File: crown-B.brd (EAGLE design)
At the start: 302 x 51.5 mm, 15 parts

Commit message: Made B board, looks a bit funky on the routing.
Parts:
- moved PTH2 7.62 mm to (43.9, 58.4)
- moved SKIP-PTH2 7.62 mm to (48.5, 47.5)
- moved C3 7.62 mm to (45.5, 39.6)
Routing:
- net VLIVE: track 179.6 -> 172.0 mm
- net PTH-DO: track 48.9 -> 41.3 mm
- net GND: track 172.9 -> 165.3 mm
- net N$5: track 67.8 -> 65.1 mm
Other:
- outline, holes or cut-outs redrawn

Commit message: Added B plate, which holds battery (best for lipo)
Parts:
- added CN2: (no value), adafruit:JST-PH-2-SMT-RA
- added U$1, U$3, U$4, U$5, U$6, U$7: SMD_BREADBOARD, pcb_crown:SMD_BREADBOARD_4X
- added U$10, U$11, U$12, U$13, U$14, U$15, U$16, U$17, U$22, U$23, U$24, U$25, U$26, U$27, U$28, U$29, U$34, U$35, U$36, U$37, U$38, U$39, U$40, U$41, U$42, U$43, U$44, U$45, U$46, U$47, U$48, U$49, U$50, U$51, U$52, U$53, U$54, U$55, U$56, U$57, U$58, U$59, U$62, U$63, U$64, U$65, U$68, U$69, U$70, U$71: SMD_PAD, pcb_crown:SMD_BREADBOARD_PAD
- moved C3 11.8 mm to (38.7, 49.3), turned to 270 degrees
- moved SKIP-PTH1 10.0 mm to (19.6, 51.6), turned to 90 degrees
- moved C4 9.24 mm to (19.8, 47.5), turned to 90 degrees
- moved SKIP-PTH2 4.61 mm to (49.1, 52.1)
- moved PTH2 0.15 mm to (43.8, 58.4)
- moved PTH1 0.13 mm to (14.5, 58.4)
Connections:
- net PTH-DI renamed PB1
- net SMD-DI renamed PB0
- new net A0: U$2.P$13, U$2.P$32, U$44.P$1, U$55.P$1
- new net A1: U$2.P$14, U$2.P$33, U$43.P$1, U$56.P$1
- new net A2: U$2.P$15, U$2.P$34, U$42.P$1, U$58.P$1
- new net N$11: U$14.P$1, U$15.P$1, U$5.P$3, U$57.P$1
- new net N$12: U$12.P$1, U$13.P$1, U$50.P$1, U$6.P$3
- new net N$13: U$10.P$1, U$11.P$1, U$49.P$1, U$7.P$3
- new net N$14: U$40.P$1, U$41.P$1, U$7.P$7, U$71.P$1
- new net N$15: U$38.P$1, U$39.P$1, U$6.P$7, U$70.P$1
- new net N$16: U$36.P$1, U$37.P$1, U$5.P$7, U$69.P$1
- new net N$17: U$34.P$1, U$35.P$1, U$4.P$7, U$68.P$1
- new net N$2: U$1.P$3, U$24.P$1, U$25.P$1, U$63.P$1
- new net N$20: U$28.P$1, U$29.P$1, U$3.P$7, U$65.P$1
- new net N$21: U$1.P$7, U$26.P$1, U$27.P$1, U$64.P$1
- new net N$22: U$2.P$35
- new net N$6: U$22.P$1, U$23.P$1, U$3.P$3, U$62.P$1
- new net N$9: U$16.P$1, U$17.P$1, U$4.P$3, U$59.P$1
- new net PB2: U$2.P$28, U$2.P$9, U$48.P$1, U$51.P$1
- new net PB3: U$2.P$10, U$2.P$29, U$47.P$1, U$52.P$1
- new net PB4: U$2.P$11, U$2.P$30, U$46.P$1, U$53.P$1
- new net PB5: U$2.P$12, U$2.P$31, U$45.P$1, U$54.P$1
- net GND: now also CN2.2, U$1.P$2, U$2.P$18, U$2.P$37, U$3.P$2, U$4.P$2, U$5.P$2, U$6.P$2, U$7.P$2
- net N$4: now also U$2.P$19
- net PTH-DO: now also U$2.P$38
- net VBAT: now also CN2.1, U$2.P$16
- net VLIVE: now also U$1.P$1, U$2.P$17, U$2.P$36, U$3.P$1, U$4.P$1, U$5.P$1, U$6.P$1, U$7.P$1
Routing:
- net VBAT: track 109.0 -> 295.6 mm, vias 1 -> 3
- net VLIVE: track 172.0 -> 289.4 mm, vias 7 -> 6
- net A2: track 0.00 -> 114.6 mm
- net A1: track 0.00 -> 110.7 mm
- net A0: track 0.00 -> 105.5 mm
- net PB5: track 0.00 -> 103.9 mm
- net PB4: track 0.00 -> 100.6 mm
- net PB3: track 0.00 -> 97.3 mm
- net PB2: track 0.00 -> 93.7 mm
- net GND: track 165.3 -> 213.9 mm, vias 7 -> 5
- net N$4: track 44.6 -> 66.6 mm
- net N$5: track 65.1 -> 44.1 mm
- net PTH-DO: track 41.3 -> 54.7 mm
- net N$9: track 0.00 -> 7.62 mm
- net N$6: track 0.00 -> 7.62 mm
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- added copper zone on layer 1, net GND
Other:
- board size 302 x 51.5 mm -> 57.8 x 50.8 mm
- board text added: "3x Alkaline"
- board text added: "4xNiCAD"
- board text added: "4xNimH"
- board text added: "A4"
- board text added: "A5"
- board text added: "D3"
- board text added: "D4"
- board text added: "D5"
- board text added: "I2C"
- board text added: "LiPo"
- board text added: "RXI"
- board text added: "TXO"

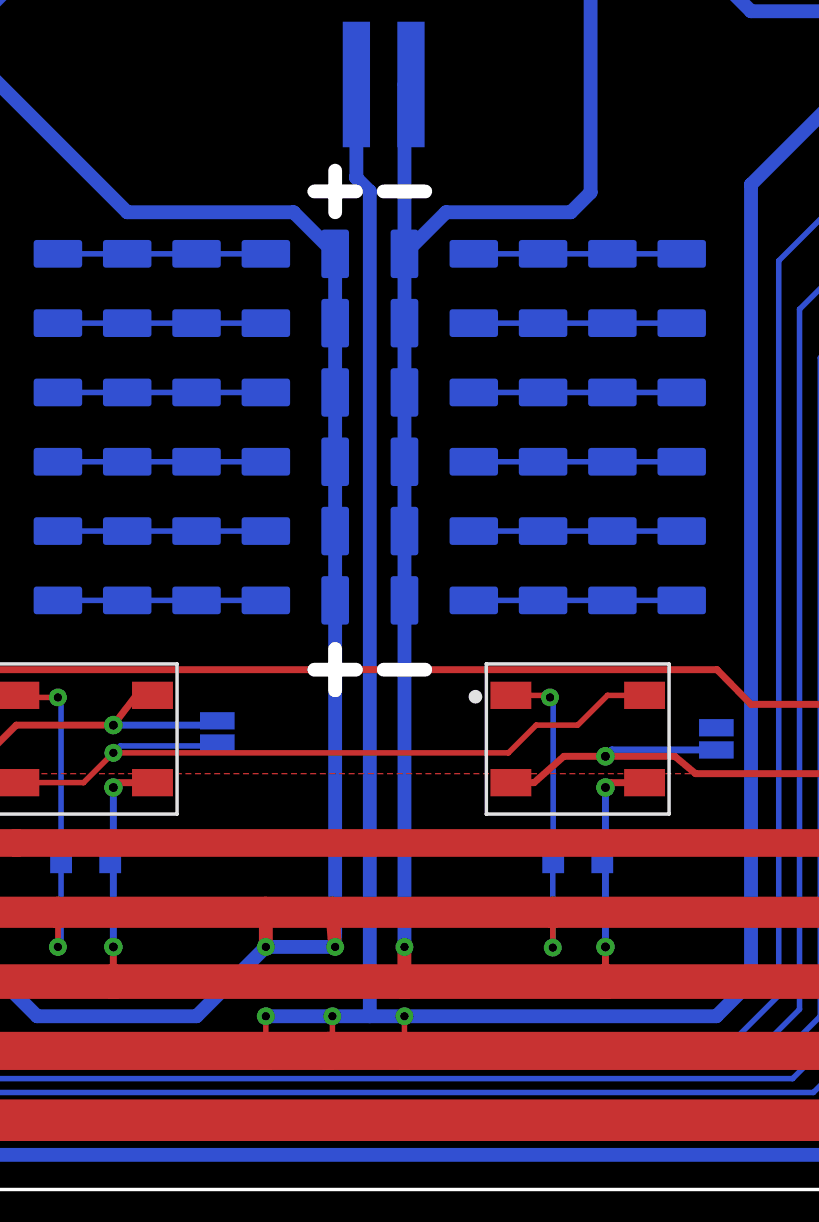
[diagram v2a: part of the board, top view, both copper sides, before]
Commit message: fixed dimension issue
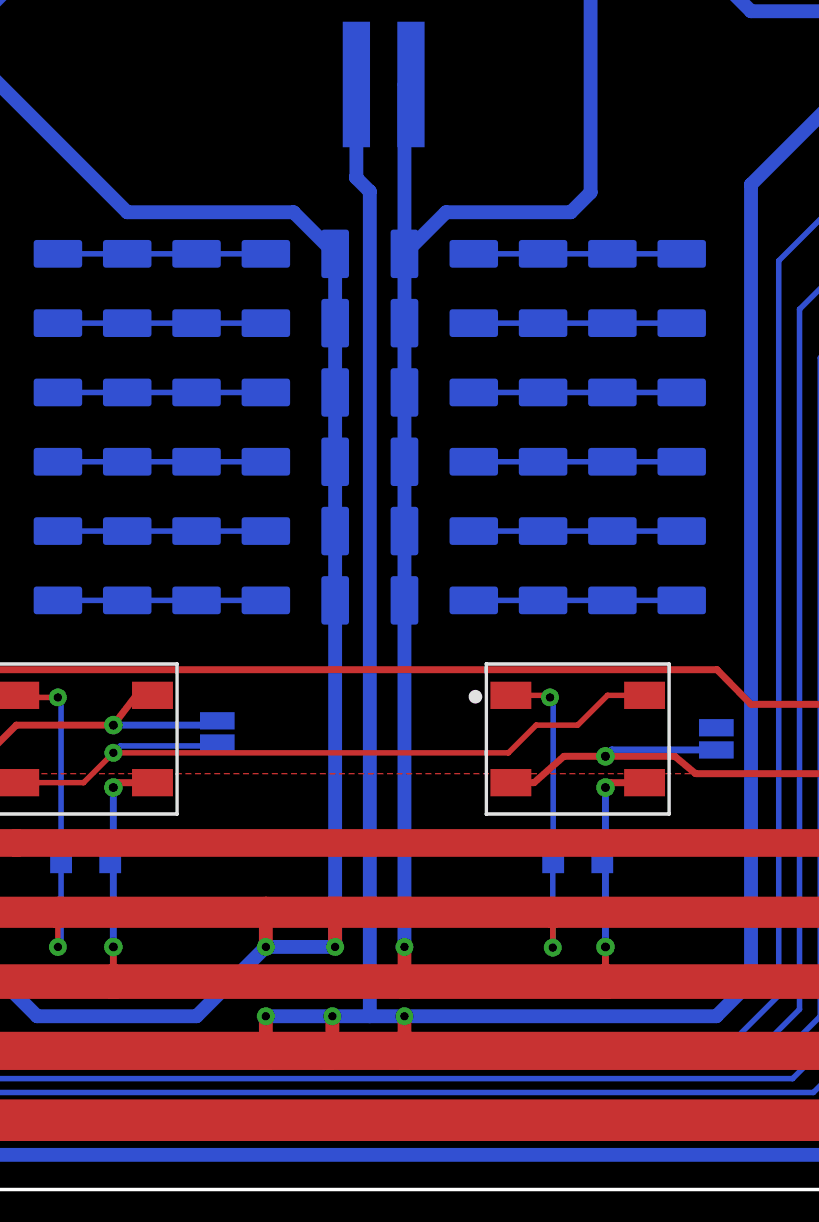
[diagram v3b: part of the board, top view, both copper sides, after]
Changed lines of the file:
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@@
 <grid distance="10" unitdist="mil" unit="mil" style="lines" multiple="5" display="yes" altdistance="1" altunitdist="mil" altunit="mil"/>
 <layers>
-<layer number="1" name="Top" color="4" fill="1" visible="no" active="yes"/>
+<layer number="1" name="Top" color="4" fill="1" visible="yes" active="yes"/>
 <layer number="16" name="Bottom" color="1" fill="1" visible="yes" active="yes"/>
 <layer number="17" name="Pads" color="2" fill="1" visible="yes" active="yes"/>
@@
 <layer number="19" name="Unrouted" color="6" fill="1" visible="yes" active="yes"/>
 <layer number="20" name="Dimension" color="15" fill="1" visible="yes" active="yes"/>
-<layer number="21" name="tPlace" color="16" fill="1" visible="no" active="yes"/>
+<layer number="21" name="tPlace" color="16" fill="1" visible="yes" active="yes"/>
 <layer number="22" name="bPlace" color="14" fill="1" visible="yes" active="yes"/>
 <layer number="23" name="tOrigins" color="15" fill="1" visible="yes" active="yes"/>
 <layer number="24" name="bOrigins" color="15" fill="1" visible="yes" active="yes"/>
 <layer number="25" name="tNames" color="7" fill="1" visible="no" active="yes"/>
-<layer number="26" name="bNames" color="7" fill="1" visible="yes" active="yes"/>
+<layer number="26" name="bNames" color="7" fill="1" visible="no" active="yes"/>
 <layer number="27" name="tValues" color="7" fill="1" visible="no" active="yes"/>
 <layer number="28" name="bValues" color="7" fill="1" visible="no" active="yes"/>
 <layer number="29" name="tStop" color="7" fill="3" visible="no" active="yes"/>
-<layer number="30" name="bStop" color="7" fill="6" visible="yes" active="yes"/>
+<layer number="30" name="bStop" color="7" fill="6" visible="no" active="yes"/>
 <layer number="31" name="tCream" color="7" fill="4" visible="no" active="yes"/>
 <layer number="32" name="bCream" color="7" fill="5" visible="no" active="yes"/>
@@
 <layer number="43" name="vRestrict" color="2" fill="10" visible="no" active="yes"/>
 <layer number="44" name="Drills" color="7" fill="1" visible="no" active="yes"/>
-<layer number="45" name="Holes" color="7" fill="1" visible="no" active="yes"/>
+<layer number="45" name="Holes" color="7" fill="1" visible="yes" active="yes"/>
 <layer number="46" name="Milling" color="3" fill="1" visible="no" active="yes"/>
 <layer number="47" name="Measures" color="7" fill="1" visible="no" active="yes"/>
@@
 <layer number="49" name="Reference" color="7" fill="1" visible="no" active="yes"/>
 <layer number="50" name="dxf" color="7" fill="1" visible="no" active="no"/>
-<layer number="51" name="tDocu" color="6" fill="1" visible="no" active="yes"/>
-<layer number="52" name="bDocu" color="7" fill="1" visible="yes" active="yes"/>
+<layer number="51" name="tDocu" color="6" fill="1" visible="yes" active="yes"/>
+<layer number="52" name="bDocu" color="7" fill="1" visible="no" active="yes"/>
 <layer number="53" name="tGND_GNDA" color="7" fill="9" visible="no" active="no"/>
 <layer number="54" name="bGND_GNDA" color="1" fill="9" visible="no" active="no"/>
@@
 <wire x1="45.72" y1="34.29" x2="44.958" y2="34.29" width="0.2032" layer="22"/>
 <wire x1="44.958" y1="34.29" x2="44.958" y2="34.036" width="0.2032" layer="22"/>
-<wire x1="29.21" y1="37.338" x2="29.21" y2="35.814" width="0.508" layer="20"/>
-<wire x1="28.448" y1="36.576" x2="29.972" y2="36.576" width="0.508" layer="20"/>
-<wire x1="30.988" y1="36.576" x2="32.512" y2="36.576" width="0.508" layer="20"/>
-<wire x1="28.448" y1="19.05" x2="29.972" y2="19.05" width="0.508" layer="20"/>
-<wire x1="29.21" y1="19.812" x2="29.21" y2="18.288" width="0.508" layer="20"/>
-<wire x1="30.988" y1="19.05" x2="32.512" y2="19.05" width="0.508" layer="20"/>
+<wire x1="29.21" y1="37.338" x2="29.21" y2="35.814" width="0.508" layer="22"/>
+<wire x1="28.448" y1="36.576" x2="29.972" y2="36.576" width="0.508" layer="22"/>
+<wire x1="30.988" y1="36.576" x2="32.512" y2="36.576" width="0.508" layer="22"/>
+<wire x1="28.448" y1="19.05" x2="29.972" y2="19.05" width="0.508" layer="22"/>
+<wire x1="29.21" y1="19.812" x2="29.21" y2="18.288" width="0.508" layer="22"/>
+<wire x1="30.988" y1="19.05" x2="32.512" y2="19.05" width="0.508" layer="22"/>
 <text x="25.4" y="45.72" size="0.889" layer="22" font="vector" ratio="15" rot="MR0">LiPo</text>
 <text x="25.4" y="43.18" size="0.889" layer="22" font="vector" ratio="15" rot="MR0">4xNiCAD</text>
@@
 <contactref element="C2" pad="1"/>
 <wire x1="19.05" y1="10.16" x2="26.67" y2="10.16" width="1.143" layer="1"/>
-<wire x1="26.67" y1="10.16" x2="29.1084" y2="10.16" width="1.143" layer="1"/>
-<wire x1="29.1084" y1="10.16" x2="37.1856" y2="10.16" width="1.143" layer="1"/>
+<wire x1="26.67" y1="10.16" x2="29.21" y2="10.16" width="1.143" layer="1"/>
+<wire x1="29.21" y1="10.16" x2="37.1856" y2="10.16" width="1.143" layer="1"/>
 <wire x1="37.1856" y1="10.16" x2="56.5912" y2="10.16" width="1.143" layer="1"/>
 <wire x1="19.166" y1="12.192" x2="19.166" y2="8.89" width="0.2032" layer="16"/>
@@
 <wire x1="37.1856" y1="8.8646" x2="37.1856" y2="10.16" width="0.2032" layer="1"/>
 <via x="29.21" y="8.89" extent="1-16" drill="0.3048"/>
-<wire x1="29.21" y1="8.89" x2="29.1084" y2="10.16" width="0.508" layer="1"/>
+<wire x1="29.21" y1="8.89" x2="29.21" y2="10.16" width="0.508" layer="1"/>
 <contactref element="U$2" pad="P$17"/>
 <wire x1="0.254" y1="43.18" x2="11.43" y2="43.18" width="0.508" layer="16"/>
@@
 <via x="29.1084" y="6.35" extent="1-16" drill="0.3048"/>
 <via x="31.75" y="6.35" extent="1-16" drill="0.3048"/>
-<wire x1="26.67" y1="6.35" x2="26.67" y2="5.08" width="0.2032" layer="1"/>
-<wire x1="31.75" y1="6.35" x2="31.75" y2="5.08" width="0.2032" layer="1"/>
-<wire x1="29.1084" y1="6.35" x2="29.1084" y2="5.2324" width="0.2032" layer="1"/>
+<wire x1="26.67" y1="6.35" x2="26.67" y2="5.08" width="0.508" layer="1"/>
+<wire x1="31.75" y1="6.35" x2="31.75" y2="5.08" width="0.508" layer="1"/>
+<wire x1="29.1084" y1="6.35" x2="29.1084" y2="5.2324" width="0.508" layer="1"/>
 <wire x1="29.1084" y1="5.2324" x2="28.956" y2="5.08" width="0.2032" layer="1"/>
 <wire x1="26.67" y1="6.35" x2="30.48" y2="6.35" width="0.508" layer="16"/>
